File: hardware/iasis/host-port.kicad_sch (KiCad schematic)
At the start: 17 parts, among them J901 1054500101, U901 TPD4E02B04DQAR, U902 TPD4E02B04DQAR, U903 HD3SS3212IRKSR, U904 TPD6S300ARUKR, U905 FUSB302BMPX

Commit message: Wire the schematic islands and side-match the RP2354 GPIOs
Each sheet now draws its circuits with wires. Labels remain at block edges
and on single-part islands: buttons, test points, decoupling and pull
resistors. The target-port page wires its hierarchical labels straight to
the child sheet pins, the ports page points its labels away from each
block, and the root sheet keeps every block clear of the title block.

The RP2354B GPIOs are reassigned so each signal leaves the package on the
side facing its destination. Update PCB from Schematic applied the 43
U1101 pad-net changes with no geometry change. Otherwise the netlist
matches the previous design, ERC keeps its 14 existing warnings and DRC
reports no parity issues.
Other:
- moved on the sheet: R904

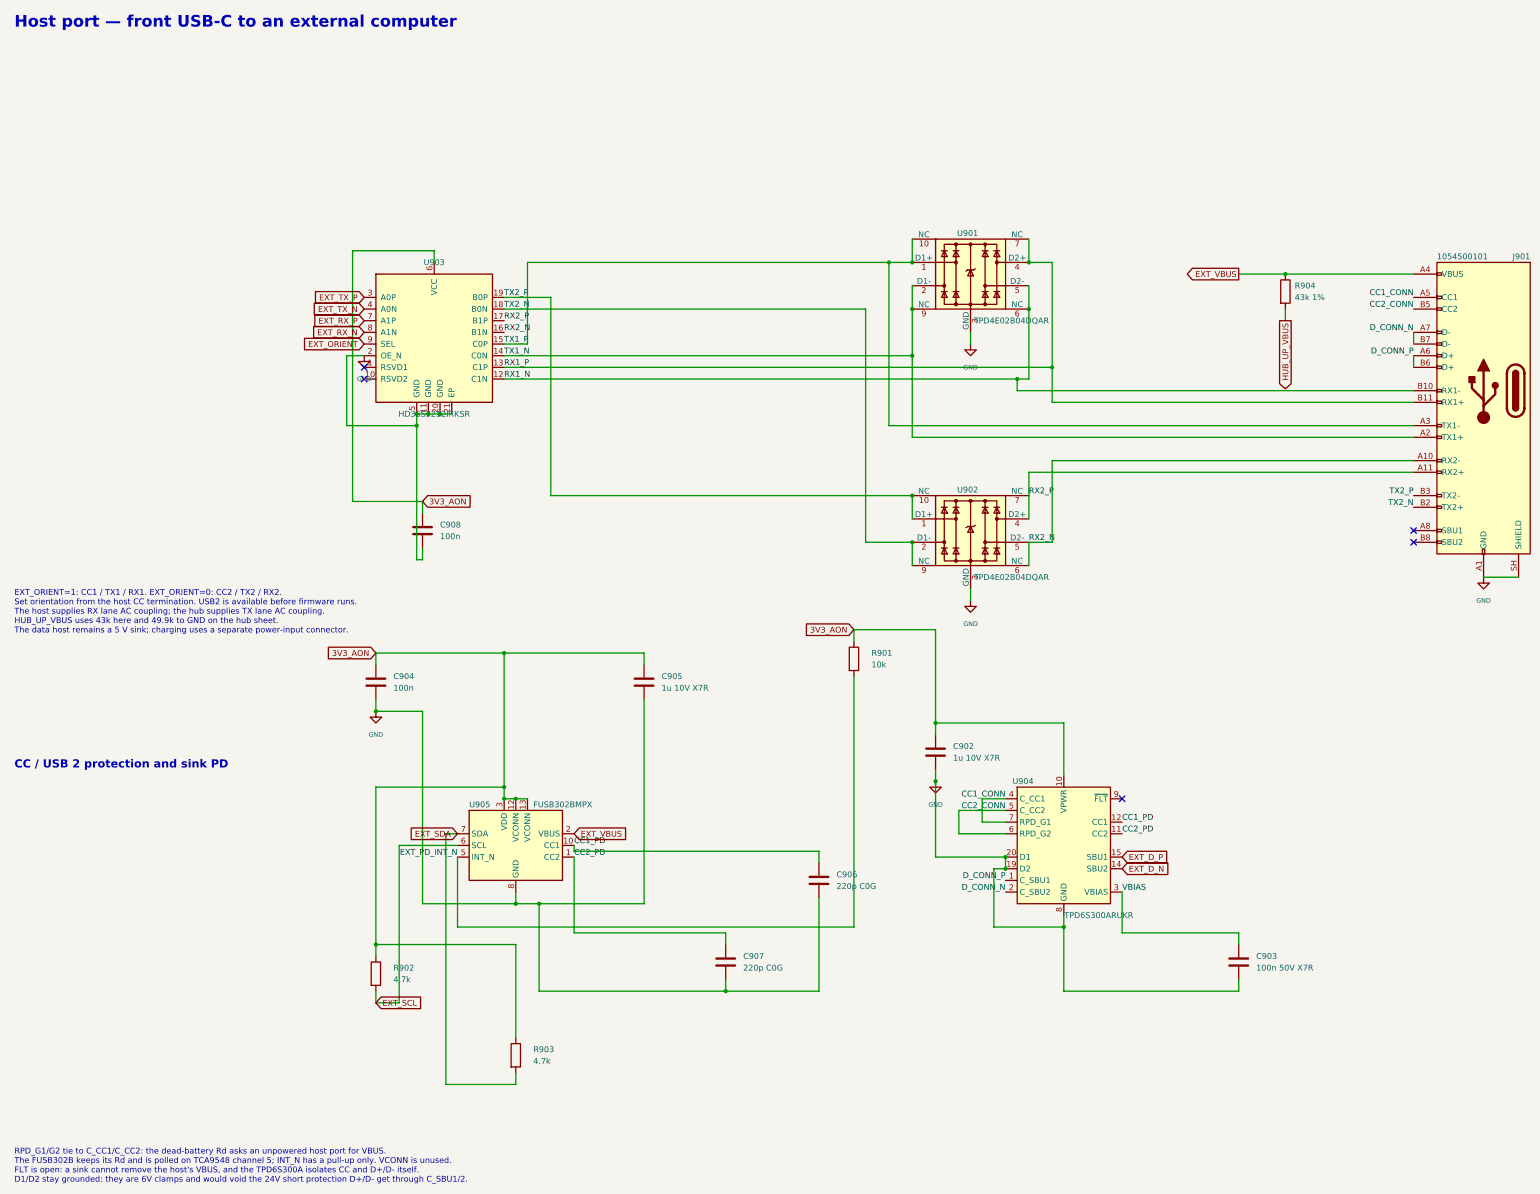
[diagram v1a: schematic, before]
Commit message: Redraw the host port and hub sheets
The host port mirrors the target data sheet. On the hub sheet the
VDD33 and VCORE pins tie to rails above the chip with their decoupling
on each rail, the crystal hangs under XI and XO, and the strap and
port-control resistors stand in banks on GND and 3V3_AON.

The USB7206C symbol's supply pins move up 2.54 mm so their names clear
the corner pin names. Pin numbers and electrical types are unchanged,
and the netlist is unchanged.
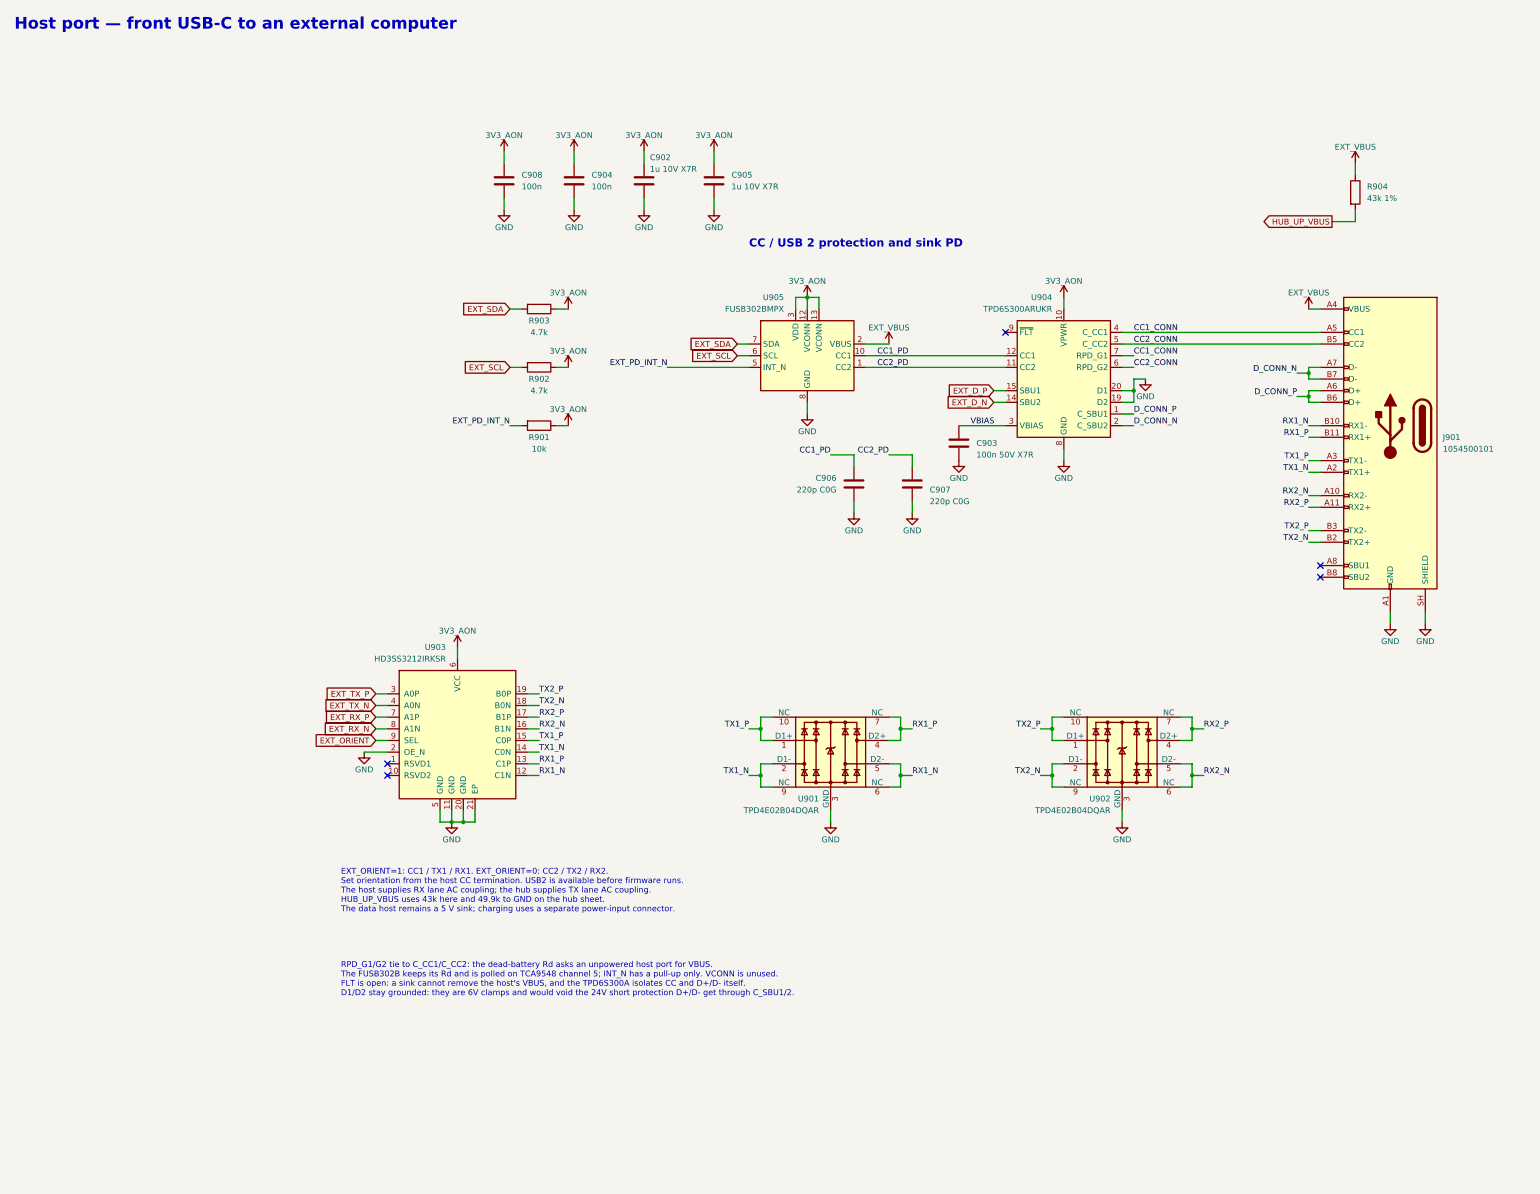
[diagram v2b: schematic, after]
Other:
- title: (none) -> Host port — front USB-C to an external computer
- moved on the sheet: C902, C903, C904, C905, C906, C907, C908, J901, R901, R902, R903, R904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

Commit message: Drill every via and thermal via at 0.3 mm
JLC prices 0.2 and 0.25 mm holes as a small-via tier that also forces
TG155 and a 4-wire Kelvin test: $39.18 on a five-board order. With
every plated hole at 0.3 mm or more the board quotes in the standard
tier.

- 2,005 vias keep their pads (0.45, 0.55, 0.6 mm) and drill 0.3 mm.
- U201's VQFN-100, the WQFN-20 and the HTSSOP-16 ThermalVias
  footprints move to Iasis.pretty copies with 0.3 mm thermal vias
  (121 holes); the schematic links follow.
- Rules match JLC's published via limits: 0.2 mm via hole to copper
  and hole to hole, 0.075 mm annular ring, 0.3 mm minimum hole.

DRC with refill and parity: 0 errors, 0 warnings, 0 unconnected.
Pour island counts unchanged; ERC unchanged at 14.
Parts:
- U904: footprint Package_DFN_QFN:WQFN-20-1EP_3x3mm_P0.4mm_EP1.7x1.7mm_ThermalVias -> Iasis:WQFN-20-1EP_3x3mm_P0.4mm_EP1.7x1.7mm_ThermalVias
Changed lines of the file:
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@@
 			)
 		)
-		(property "Footprint" "Package_DFN_QFN:WQFN-20-1EP_3x3mm_P0.4mm_EP1.7x1.7mm_ThermalVias"
+		(property "Footprint" "Iasis:WQFN-20-1EP_3x3mm_P0.4mm_EP1.7x1.7mm_ThermalVias"
 			(at 254 99.06 0)
 			(hide yes)

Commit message: fix: correct core power and recovery circuitry
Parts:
- removed R904: 43k 1%, Resistor_SMD:R_0402_1005Metric, symbol Device:R
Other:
- note added: "EXT_ORIENT=1: CC1 / TX1 / RX1. EXT_ORIENT=0: CC2 / TX2 / RX2. Set orientation from the host CC termination. USB2 is available before firmware runs. The host supplies RX lane AC coupling; the hub supplies TX lane AC coupling. Logic is host-powered; the hub VBUS detect follows its own 3.3 V supply. The data host remains a 5 V sink; charging uses a separate power-input connector."
- note removed: "EXT_ORIENT=1: CC1 / TX1 / RX1. EXT_ORIENT=0: CC2 / TX2 / RX2. Set orientation from the host CC termination. USB2 is available before firmware runs. The host supplies RX lane AC coupling; the hub supplies TX lane AC coupling. HUB_UP_VBUS uses 43k here and 49.9k to GND on the hub sheet. The data host remains a 5 V sink; charging uses a separate power-input connector."
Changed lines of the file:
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@@
 		)
 	)
-	(text "EXT_ORIENT=1: CC1 / TX1 / RX1. EXT_ORIENT=0: CC2 / TX2 / RX2.\nSet orientation from the host CC termination. USB2 is available before firmware runs.\nThe host supplies RX lane AC coupling; the hub supplies TX lane AC coupling.\nHUB_UP_VBUS uses 43k here and 49.9k to GND on the hub sheet.\nThe data host remains a 5 V sink; charging uses a separate power-input connector."
+	(text "EXT_ORIENT=1: CC1 / TX1 / RX1. EXT_ORIENT=0: CC2 / TX2 / RX2.\nSet orientation from the host CC termination. USB2 is available before firmware runs.\nThe host supplies RX lane AC coupling; the hub supplies TX lane AC coupling.\nLogic is host-powered; the hub VBUS detect follows its own 3.3 V supply.\nThe data host remains a 5 V sink; charging uses a separate power-input connector."
 		(exclude_from_sim no)
 		(at 96.52 205.74 0)
@@
 	(wire
 		(pts
-			(xy 317.5 62.23) (xy 317.5 64.77)
-		)
-		(stroke
-			(width 0)
-			(type default)
-		)
-	)
-	(wire
-		(pts
 			(xy 307.34 97.79) (xy 304.8 97.79)
 		)
@@
 	(wire
 		(pts
-			(xy 317.5 64.77) (xy 312.42 64.77)
-		)
-		(stroke
-			(width 0)
-			(type default)
-		)
-	)
-	(wire
-		(pts
 			(xy 132.08 59.69) (xy 132.08 62.23)
 		)
@@
 	(wire
 		(pts
-			(xy 317.5 54.61) (xy 317.5 52.07)
-		)
-		(stroke
-			(width 0)
-			(type default)
-		)
-	)
-	(wire
-		(pts
 			(xy 281.94 175.26) (xy 281.94 177.8)
 		)
@@
 		)
 	)
-	(global_label "HUB_UP_VBUS"
-		(shape output)
-		(at 312.42 64.77 180)
-		(effects
-			(font
-				(size 1.27 1.27)
-			)
-			(justify right)
-		)
-		(property "Intersheetrefs" "${INTERSHEET_REFS}"
-			(at 312.42 64.77 0)
-			(hide yes)
-			(show_name no)
-			(do_not_autoplace no)
-			(effects
-				(font
-					(size 1.27 1.27)
-				)
-			)
-		)
-	)
 	(global_label "EXT_SDA"
 		(shape input)
@@
 	)
 	(symbol
-		(lib_id "power:VBUS")
-		(at 317.5 52.07 0)
-		(unit 1)
-		(body_style 1)
-		(exclude_from_sim no)
-		(in_bom yes)
-		(on_board yes)
-		(in_pos_files yes)
-		(dnp no)
-		(property "Reference" "#PWR2594004"
-			(at 317.5 52.07 0)
-			(hide yes)
-			(show_name no)
-			(do_not_autoplace no)
-			(effects
-				(font
-					(size 1.27 1.27)
-				)
-			)
-		)
-		(property "Value" "EXT_VBUS"
-			(at 317.5 48.514 0)
-			(show_name no)
-			(do_not_autoplace no)
-			(effects
-				(font
-					(size 1.27 1.27)
-				)
-			)
-		)
-		(property "Footprint" ""
-			(at 317.5 52.07 0)
-			(hide yes)
-			(show_name no)
-			(do_not_autoplace no)
-			(effects
-				(font
-					(size 1.27 1.27)
-				)
-			)
-		)
-		(property "Datasheet" ""
-			(at 317.5 52.07 0)
-			(hide yes)
-			(show_name no)
-			(do_not_autoplace no)
-			(effects
-				(font
-					(size 1.27 1.27)
-				)
-			)
-		)
-		(property "Description" ""
-			(at 317.5 52.07 0)
-			(show_name no)
-			(do_not_autoplace no)
-			(effects
-				(font
-					(size 1.27 1.27)
-				)
-			)
-		)
-		(pin "1"
-		)
-		(instances
-			(project "iasis"
-				(path "/a379403c-5d83-493f-982e-fb5e1b803ee5/a8cd007d-22b6-4951-9feb-b8af9e75802d"
-					(reference "#PWR2594004")
-					(unit 1)
-				)
-			)
-		)
-	)
-	(symbol
 		(lib_id "Iasis:TPD4E02B04DQA")
 		(at 266.7 180.34 0)
@@
 					(unit 1)
 				)
-			)
-		)
-	)
-	(symbol
-		(lib_id "Device:R")
-		(at 317.5 58.42 0)
-		(unit 1)
-		(body_style 1)
-		(exclude_from_sim no)
-		(in_bom yes)
-		(on_board yes)
-		(in_pos_files yes)
-		(dnp no)
-		(property "Reference" "R904"
-			(at 320.04 57.15 0)
-			(show_name no)
-			(do_not_autoplace no)
-			(effects
-				(font
-					(size 1.27 1.27)
-				)
-				(justify left)
-			)
-		)
-		(property "Value" "43k 1%"
-			(at 320.04 59.69 0)
-			(show_name no)
-			(do_not_autoplace no)
-			(effects
-				(font
-					(size 1.27 1.27)
-				)
-				(justify left)
-			)
-		)
-		(property "Footprint" "Resistor_SMD:R_0402_1005Metric"
-			(at 317.5 58.42 0)
-			(hide yes)
-			(show_name no)
-			(do_not_autoplace no)
-			(effects
-				(font
-					(size 1.27 1.27)
-				)
-			)
-		)
-		(property "Datasheet" "https://www.lcsc.com/datasheet/lcsc_datasheet_2206010216_UNI-ROYAL-Uniroyal-Elec-0402WGF4302TCE_C8329.pdf"
-			(at 317.5 58.42 0)
-			(hide yes)
-			(show_name no)
-			(do_not_autoplace no)
-			(effects
-				(font
-					(size 1.27 1.27)
-				)
-			)
-		)
-		(property "Description" "Resistor"
-			(at 317.5 58.42 0)
-			(hide yes)
-			(show_name no)
-			(do_not_autoplace no)
-			(effects
-				(font
-					(size 1.27 1.27)
-				)
-			)
-		)
-		(property "LCSC" "C8329"
-			(at 317.5 58.42 0)
-			(hide yes)
-			(show_name no)
-			(do_not_autoplace no)
-			(effects
-				(font
-					(size 1.27 1.27)
-				)
-			)
-		)
-		(property "MPN" "0402WGF4302TCE"
-			(at 317.5 58.42 0)
-			(hide yes)
-			(show_name no)
-			(do_not_autoplace no)
-			(effects
-				(font
-					(size 1.27 1.27)
-				)
-			)
-		)
-		(property "Manufacturer" "UNI-ROYAL(Uniroyal Elec)"
-			(at 317.5 58.42 0)
-			(hide yes)
-			(show_name no)
-			(do_not_autoplace no)
-			(effects
-				(font
-					(size 1.27 1.27)
-				)
-			)
-		)
-		(pin "2"
-		)
-		(pin "1"
-		)
-		(instances
-			(project "iasis"
-				(path "/a379403c-5d83-493f-982e-fb5e1b803ee5/a8cd007d-22b6-4951-9feb-b8af9e75802d"
-					(reference "R904")
-					(unit 1)
-				)
